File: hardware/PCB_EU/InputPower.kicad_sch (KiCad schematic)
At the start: 33 parts, among them J101 24 V IN, U101 L7987 3A

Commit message: hardware: apply PCB_EU review fixes
- R702 100k -> 4k7: ESP32 internal pull-up on GPIO32 (old firmware
  INPUT_PULLUP) could switch the 100 W PTC on.
- C208 100n -> 1u for the Espressif EN delay.
- Remove TC4427A driver and its parts; each LM3429 GATE drives its own
  IRF540Z through 4R7 (driver was 20-25 mm from both MOSFETs).
- Add reverse-polarity protection: Q102 IRF1010ES in the input return
  with a 5k6+5k6 / 10k gate divider.
- F103 label: UST 1206 is time-lag.
- Rebuild PCB via build_board.py + route_power.py, rerun all checks on
  KiCad 10.0.7: ERC 0, DRC 0 / parity 0, 355 unrouted, 51 checks.
- Parts estimate 80.00 -> 78.59 EUR; check ceiling raised to 100 EUR.

Co-Authored-By: Claude Opus 5.5 (1M context) <noreply@anthropic.com>
Claude-Session: https://claude.ai/code/session_01AxccZX6Cb4FnRKJMrFYMSX
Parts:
- added Q102: IRF1010ESPBF, Package_TO_SOT_SMD:TO-263-2, symbol EU:NMOS
- added R108, R109: 5k6 1%, Resistor_SMD:R_1206_3216Metric, symbol EU:R
- added R110: 10k 1%, Resistor_SMD:R_1206_3216Metric, symbol EU:R
- F103: value 6.3 A fast -> 6.3 A slow
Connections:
- net +24V_FUSED: now also R108.1
- net GND: now also Q102.3 (S), R110.2; no longer J101.2
- new net PSU_RTN: J101.2, Q102.2 (D)
- new net REVP_GATE: Q102.1 (G), R109.2, R110.1
- new net REVP_MID: R108.2, R109.1
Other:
- note added: "External PSU 24.0 V, max 25 V, at least 240 W / 10 A. J101: 1 = +24 V, 2 = PSU return. Reverse polarity: Q102 IRF1010ES in the return path; drain = J101.2, source = board GND. Q102 gate divider 5k6+5k6 / 10k from +24V_FUSED: Vgs 10.2 V at 21.6 V, 19.8 V at 42 V TVS clamp. Programmer/USB ground must never become the power return. Fuse coordination NOT qualified. L7987 is the 3 A part. VCC is on 24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"
- note removed: "External PSU 24.0 V, max 25 V. J101: 1 = +24 V, 2 = GND. Fuse coordination and reverse polarity survival are NOT qualified. L7987 is the 3 A part. VCC is on 24 V; VBIAS is on the regulated 12 V rail. RF + CF series from COMP to FB; CP across the complete RF/CF network. C112 has 0.1 ohm in series to GND. This is deliberate compensation damping."
- moved on the sheet: C101, C102, C103, C104, C105, C106, C107, C108, C109, C110, C111, C112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

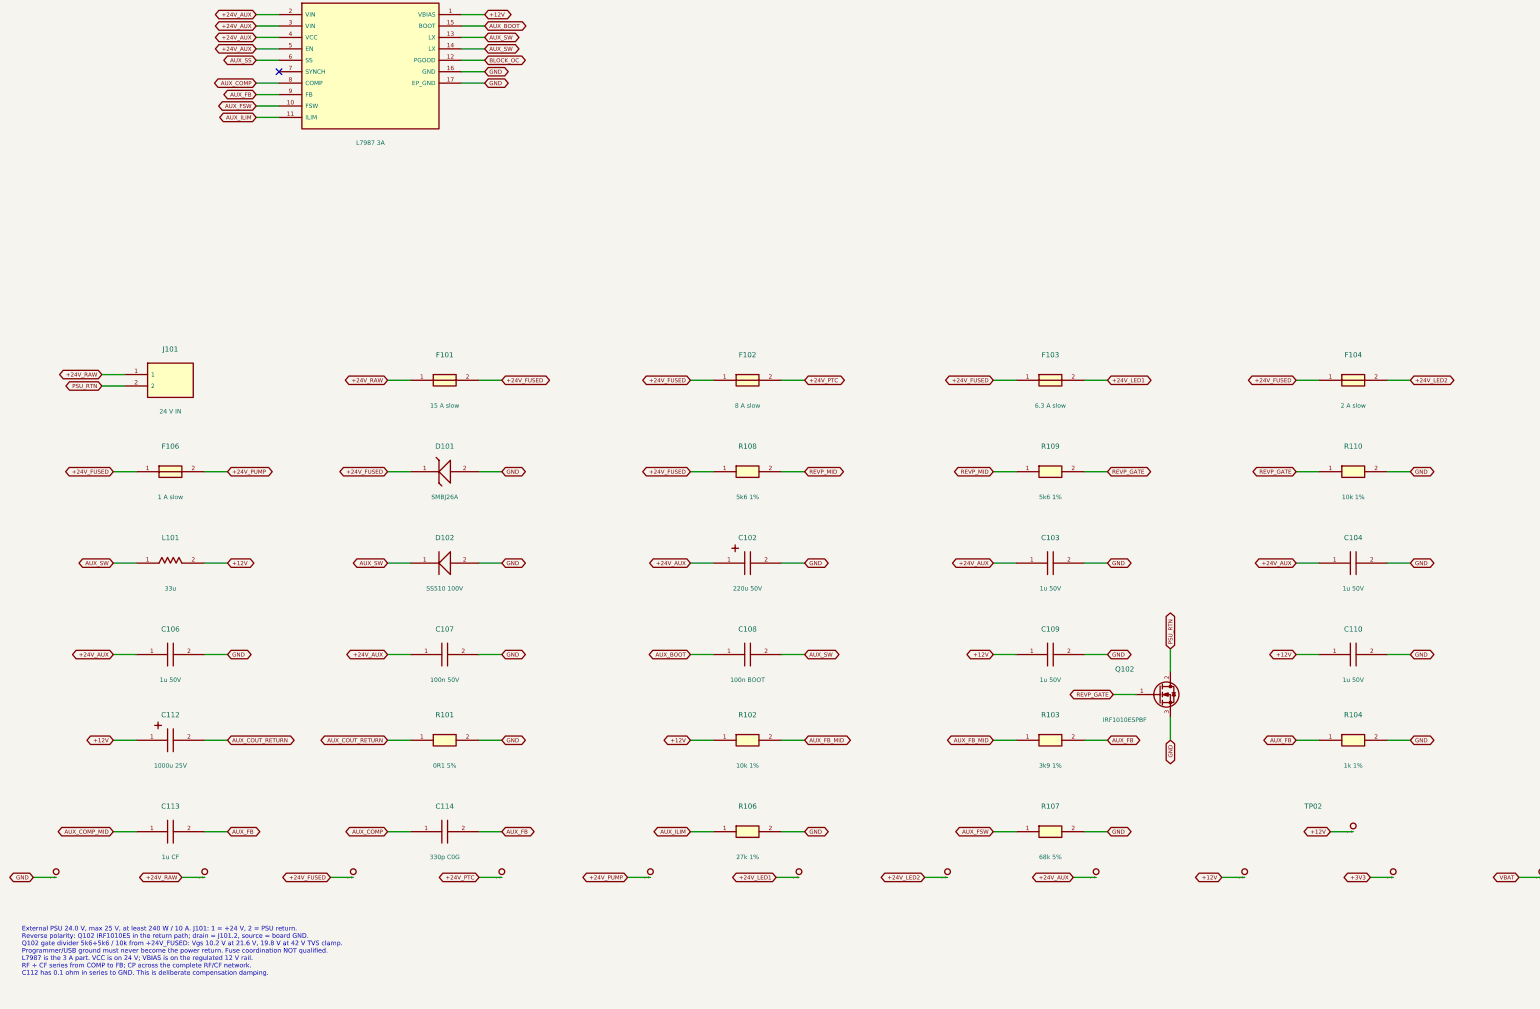
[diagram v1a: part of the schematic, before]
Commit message: PCB_EU: INA226 power monitor in the 24 V return
Adds U102 INA226 (I2C 0x40) with a 5 mOhm low-side shunt (R111 || R112,
2x 0R01 2512) between board GND and the Q102 source (new net RTN_SHUNT).
IN+/IN- are Kelvin tracks; a fill keepout keeps the GND pour off the IN+
track. VBUS is fed from +24V_FUSED through R113 1k with D103 BZV55-C33
so the D101 42 V clamp stays below the 40 V abs max. C115 decouples VS.

Board fully routed again: DRC 0, parity 0, 0 unconnected, rebuild
byte-identical. BOM EUR 82.50 (+4.55). DESIGN.md has the firmware data
(address, shunt, CAL, accuracy) and the new power-monitor section.

Co-Authored-By: Claude Sonnet 5.5 <noreply@anthropic.com>
Claude-Session: https://claude.ai/code/session_01AxccZX6Cb4FnRKJMrFYMSX
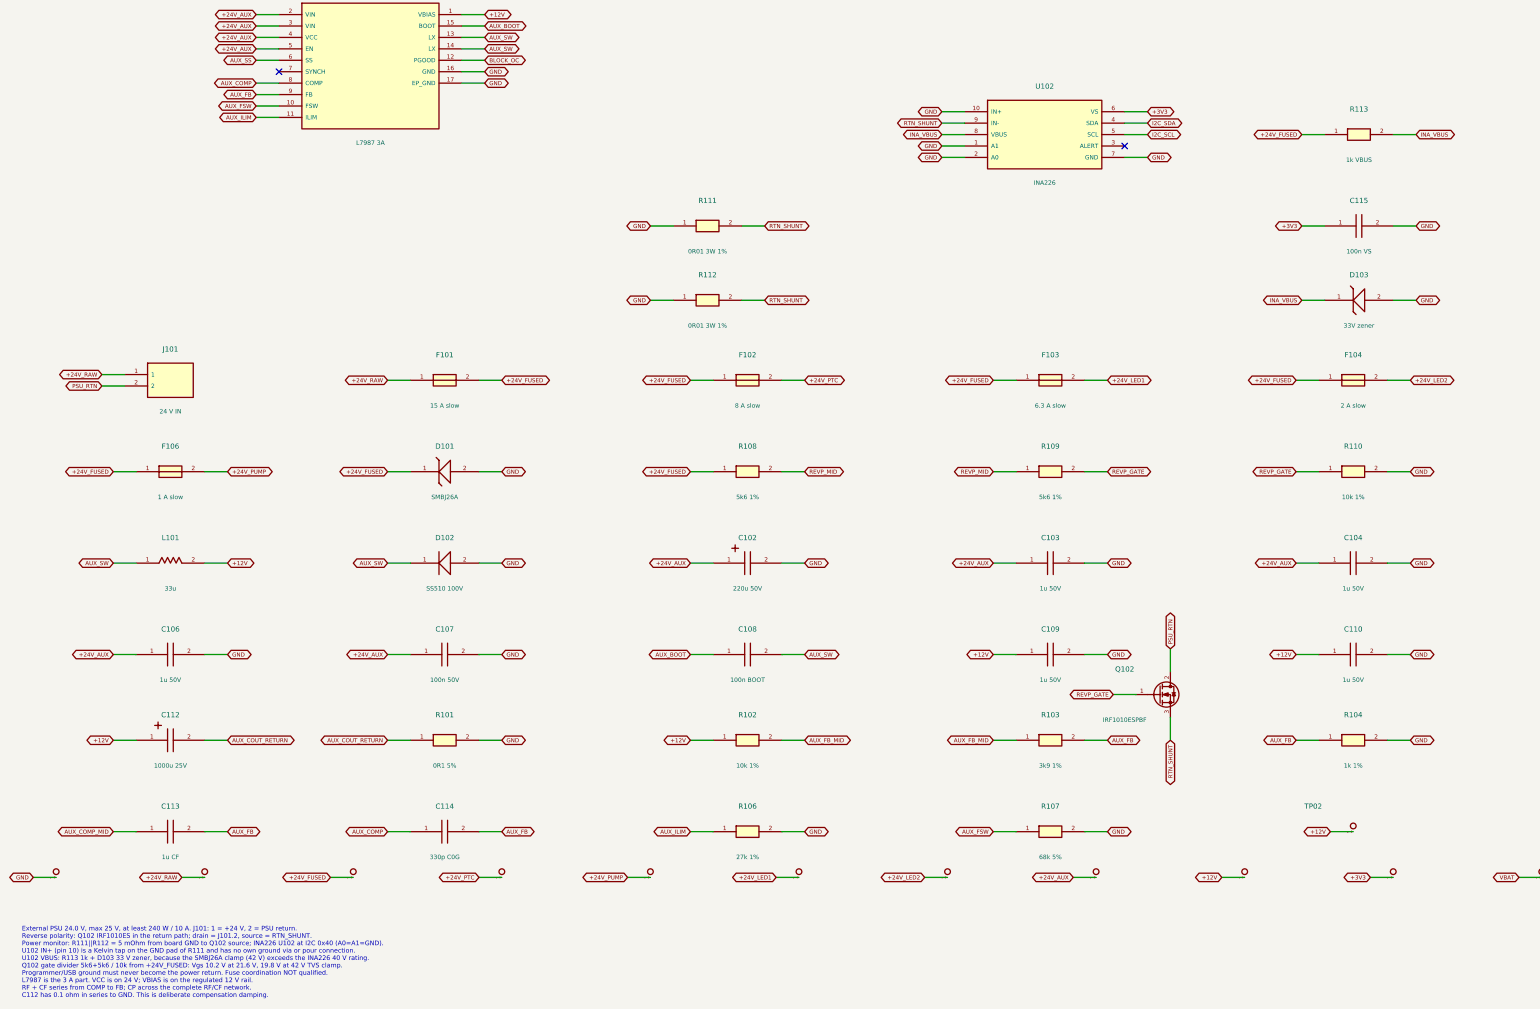
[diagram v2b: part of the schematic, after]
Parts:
- added C115: 100n VS, Capacitor_SMD:C_0805_2012Metric, symbol EU:C
- added D103: 33V zener, Diode_SMD:D_MiniMELF, symbol EU:TVS
- added R111, R112: 0R01 3W 1%, Resistor_SMD:R_2512_6332Metric, symbol EU:R
- added R113: 1k VBUS, Resistor_SMD:R_0603_1608Metric, symbol EU:R
- added U102: INA226, Package_SO:VSSOP-10_3x3mm_P0.5mm, symbol EU:INA226
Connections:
- net +24V_FUSED: now also R113.1
- net +3V3: now also C115.1, U102.6 (VS)
- net GND: now also C115.2, D103.2 (A), R111.1, R112.1, U102.1 (A1), U102.10 (IN+), U102.2 (A0), U102.7 (GND); no longer Q102.3 (S)
- new net I2C_SCL: U102.5 (SCL)
- new net I2C_SDA: U102.4 (SDA)
- new net INA_VBUS: D103.1 (K), R113.2, U102.8 (VBUS)
- new net RTN_SHUNT: Q102.3 (S), R111.2, R112.2, U102.9 (IN-)
- no-connect marks 1 -> 2
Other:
- note added: "External PSU 24.0 V, max 25 V, at least 240 W / 10 A. J101: 1 = +24 V, 2 = PSU return. Reverse polarity: Q102 IRF1010ES in the return path; drain = J101.2, source = RTN_SHUNT. Power monitor: R111||R112 = 5 mOhm from board GND to Q102 source; INA226 U102 at I2C 0x40 (A0=A1=GND). U102 IN+ (pin 10) is a Kelvin tap on the GND pad of R111 and has no own ground via or pour connection. U102 VBUS: R113 1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"
- note removed: "External PSU 24.0 V, max 25 V, at least 240 W / 10 A. J101: 1 = +24 V, 2 = PSU return. Reverse polarity: Q102 IRF1010ES in the return path; drain = J101.2, source = board GND. Q102 gate divider 5k6+5k6 / 10k from +24V_FUSED: Vgs 10.2 V at 21.6 V, 19.8 V at 42 V TVS clamp. Programmer/USB ground must never become the power return. Fuse coordination NOT qualified. L7987 is the 3 A part. VCC is on 24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"

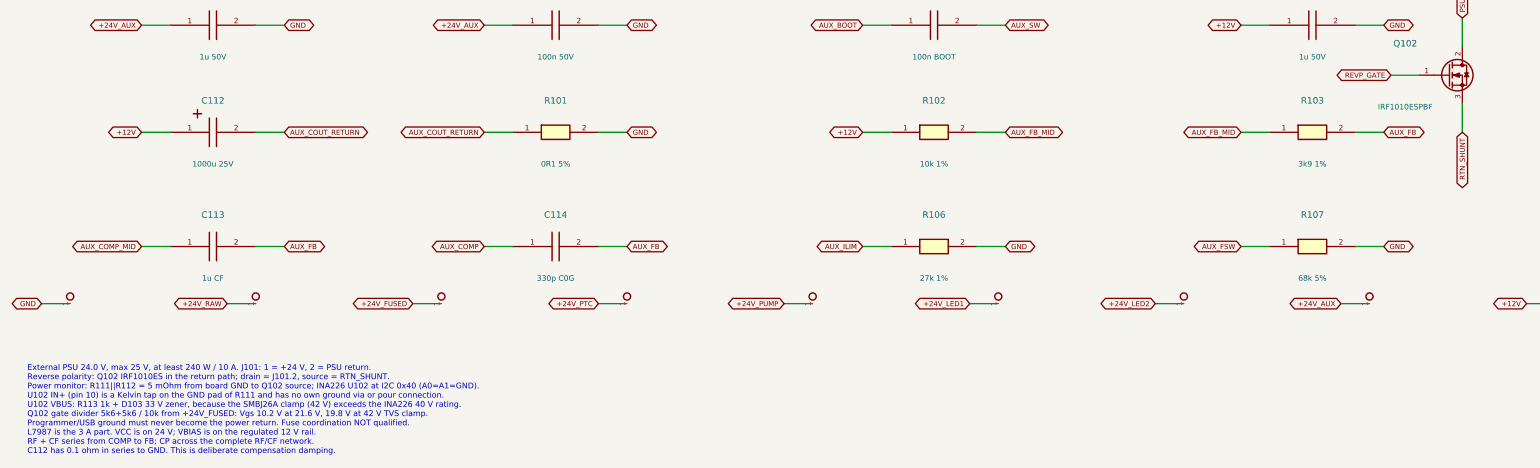
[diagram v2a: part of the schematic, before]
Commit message: PCB_EU: Q601 CSD19534KCS, Q102/Q703 FDB5800, BOM updated
Q601 (LED2 boost switch, no heatsink): TK22E10N1 -> TI CSD19534KCS on the
same TO-220 land. Q102 (reverse polarity) and Q703 (PTC switch):
IRF1010ESPBF -> onsemi FDB5800 on the same TO-263-2 land. Q501 stays
TK22E10N1.

BOM 82.50 -> 85.75 EUR: FDB5800 x2 Salvats 3.96 (was IRF 2.42),
TK22E10N1 x1 instead of x2 (-1.38), CSD19534KCS x1 Electrobase 3.09.
Shipping 5.87 and the two parcels are unchanged.

tools/generate.py rebuilds schematics, design.json and the BOM (the
generator is idempotent). Value/Datasheet/MPN/Design_note of the three
parts are text-patched in PCB_EU.kicad_pcb and review/netlist.xml the way
a KiCad export and build_board.py would write them; review/connectivity.txt
comes from tools/verify.py (56 checks pass). DESIGN.md and README.md are
updated.

KiCad was not run: ERC, DRC, schematic parity and the other KiCad-based
checks of run_checks.py have NOT been run for this commit.

Co-Authored-By: Claude Sonnet 5.5 <noreply@anthropic.com>
Claude-Session: https://claude.ai/code/session_011GxPyRnAFpBjFQ5VURqV5H
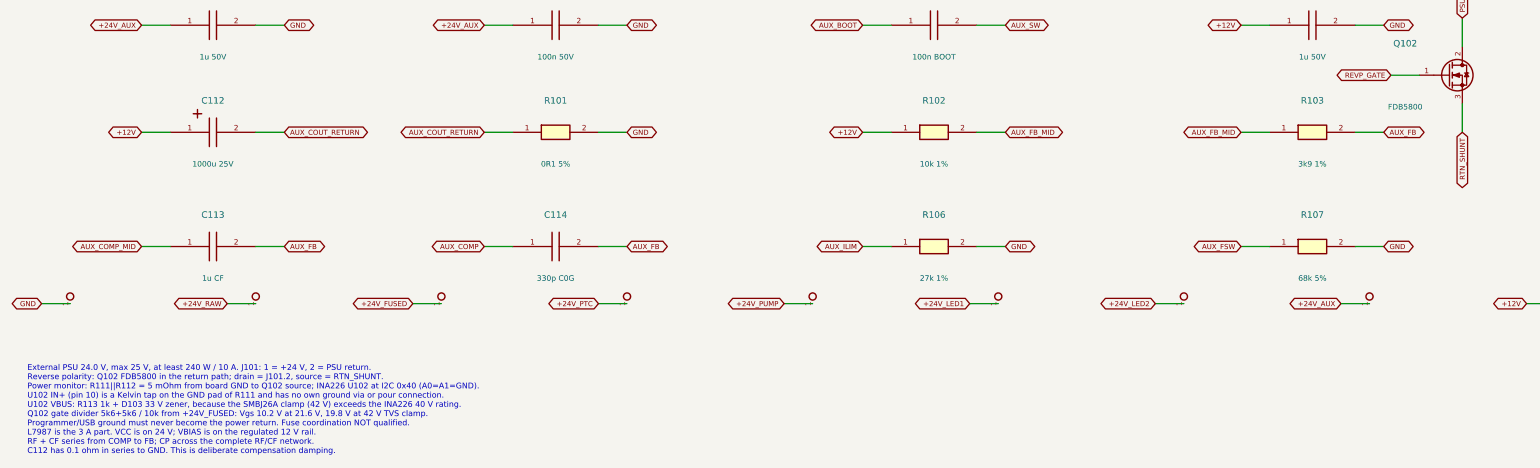
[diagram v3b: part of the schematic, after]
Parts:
- Q102: value IRF1010ESPBF -> FDB5800; MPN IRF1010ESPBF -> FDB5800
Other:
- note added: "External PSU 24.0 V, max 25 V, at least 240 W / 10 A. J101: 1 = +24 V, 2 = PSU return. Reverse polarity: Q102 FDB5800 in the return path; drain = J101.2, source = RTN_SHUNT. Power monitor: R111||R112 = 5 mOhm from board GND to Q102 source; INA226 U102 at I2C 0x40 (A0=A1=GND). U102 IN+ (pin 10) is a Kelvin tap on the GND pad of R111 and has no own ground via or pour connection. U102 VBUS: R113 1k 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"
- note removed: "External PSU 24.0 V, max 25 V, at least 240 W / 10 A. J101: 1 = +24 V, 2 = PSU return. Reverse polarity: Q102 IRF1010ES in the return path; drain = J101.2, source = RTN_SHUNT. Power monitor: R111||R112 = 5 mOhm from board GND to Q102 source; INA226 U102 at I2C 0x40 (A0=A1=GND). U102 IN+ (pin 10) is a Kelvin tap on the GND pad of R111 and has no own ground via or pour connection. U102 VBUS: R113 1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"
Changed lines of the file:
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@@
 (kicad_sch (version 20260306) (generator "eeschema") (generator_version "10.0") (paper "A3") (title_block (title "01 | 24 V input and 12 V auxiliary supply") (date "2026-10-20") (rev "EU-0.1") (company "GrowBox | EU prototype") (comment 1 "SCHEMATIC DRAFT | PARTIAL LED1 PCB ROUTING | no manufacturing release"))
 (text "01 | 24 V input and 12 V auxiliary supply" (at 12.7 12.7 0) (effects (font (size 2 2)) (justify left top)))
-(text "External PSU 24.0 V, max 25 V, at least 240 W / 10 A. J101: 1 = +24 V, 2 = PSU return.\nReverse polarity: Q102 IRF1010ES in the return path; drain = J101.2, source = RTN_SHUNT.\nPower monitor: R111||R112 = 5 mOhm from board GND to Q102 source; INA226 U102 at I2C 0x40 (A0=A1=GND).\nU102 IN+ (pin 10) is a Kelvin tap on the GND pad of R111 and has no own ground via or pour connection.\nU102 VBUS: R113 1k + D103 33 V zener, because the SMBJ26A clamp (42 V) exceeds the INA226 40 V rating.\nQ102 gate divider 5k6+5k6 / 10k from +24V_FUSED: Vgs 10.2 V at 21.6 V, 19.8 V at 42 V TVS clamp.\nProgrammer/USB ground must never become the power return. Fuse coordination NOT qualified.\nL7987 is the 3 A part. VCC is on 24 V; VBIAS is on the regulated 12 V rail.\nRF + CF series from COMP to FB; CP across the complete RF/CF network.\nC112 has 0.1 ohm in series to GND. This is deliberate compensation damping." (at 12.7 251 0) (effects (font (size 1.02 1.02)) (justify left top)))
+(text "External PSU 24.0 V, max 25 V, at least 240 W / 10 A. J101: 1 = +24 V, 2 = PSU return.\nReverse polarity: Q102 FDB5800 in the return path; drain = J101.2, source = RTN_SHUNT.\nPower monitor: R111||R112 = 5 mOhm from board GND to Q102 source; INA226 U102 at I2C 0x40 (A0=A1=GND).\nU102 IN+ (pin 10) is a Kelvin tap on the GND pad of R111 and has no own ground via or pour connection.\nU102 VBUS: R113 1k + D103 33 V zener, because the SMBJ26A clamp (42 V) exceeds the INA226 40 V rating.\nQ102 gate divider 5k6+5k6 / 10k from +24V_FUSED: Vgs 10.2 V at 21.6 V, 19.8 V at 42 V TVS clamp.\nProgrammer/USB ground must never become the power return. Fuse coordination NOT qualified.\nL7987 is the 3 A part. VCC is on 24 V; VBIAS is on the regulated 12 V rail.\nRF + CF series from COMP to FB; CP across the complete RF/CF network.\nC112 has 0.1 ohm in series to GND. This is deliberate compensation damping." (at 12.7 251 0) (effects (font (size 1.02 1.02)) (justify left top)))
 (symbol (lib_id "EU:J2") (at 45.72 129.54 0) (unit 1) (in_bom yes) (on_board yes) (dnp no)
 (property "Reference" "J101" (at 45.72 122.63 0) (effects (font (size 1.15 1.15)) ))
@@
 (symbol (lib_id "EU:NMOS") (at 265.43 199.39 0) (unit 1) (in_bom yes) (on_board yes) (dnp no)
 (property "Reference" "Q102" (at 257.81 193.75 0) (effects (font (size 1.15 1.15)) ))
-(property "Value" "IRF1010ESPBF" (at 257.81 205.03 0) (effects (font (size 0.98 0.98)) ))
+(property "Value" "FDB5800" (at 257.81 205.03 0) (effects (font (size 0.98 0.98)) ))
 (property "Footprint" "Package_TO_SOT_SMD:TO-263-2" (at 265.43 199.39 0) (effects (font (size 1 1)) (hide yes)))
-(property "Datasheet" "" (at 265.43 199.39 0) (effects (font (size 1 1)) (hide yes)))
-(property "MPN" "IRF1010ESPBF" (at 265.43 199.39 0) (effects (font (size 1 1)) (hide yes)))
+(property "Datasheet" "https://www.onsemi.com/pdf/datasheet/fdb5800-d.pdf" (at 265.43 199.39 0) (effects (font (size 1 1)) (hide yes)))
+(property "MPN" "FDB5800" (at 265.43 199.39 0) (effects (font (size 1 1)) (hide yes)))
 (property "Design_note" "Reverse-polarity switch in the 24 V return. Tab = DRAIN = PSU_RTN; body diode conducts until the gate is enhanced" (at 265.43 199.39 0) (effects (font (size 1 1)) (hide yes)))
 (property "FootprintStatus" "PACKAGE ONLY - verify before PCB" (at 265.43 199.39 0) (effects (font (size 1 1)) (hide yes)))
